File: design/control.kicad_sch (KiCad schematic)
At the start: 22 parts, among them J1 USB_C_Receptacle_USB2.0_14P, J2 SMB, J3 Conn-OScope, J4 Conn-OScope, J5 SMA, U1 CP2102N-Axx-xQFN20, U2 STM32F303RETx

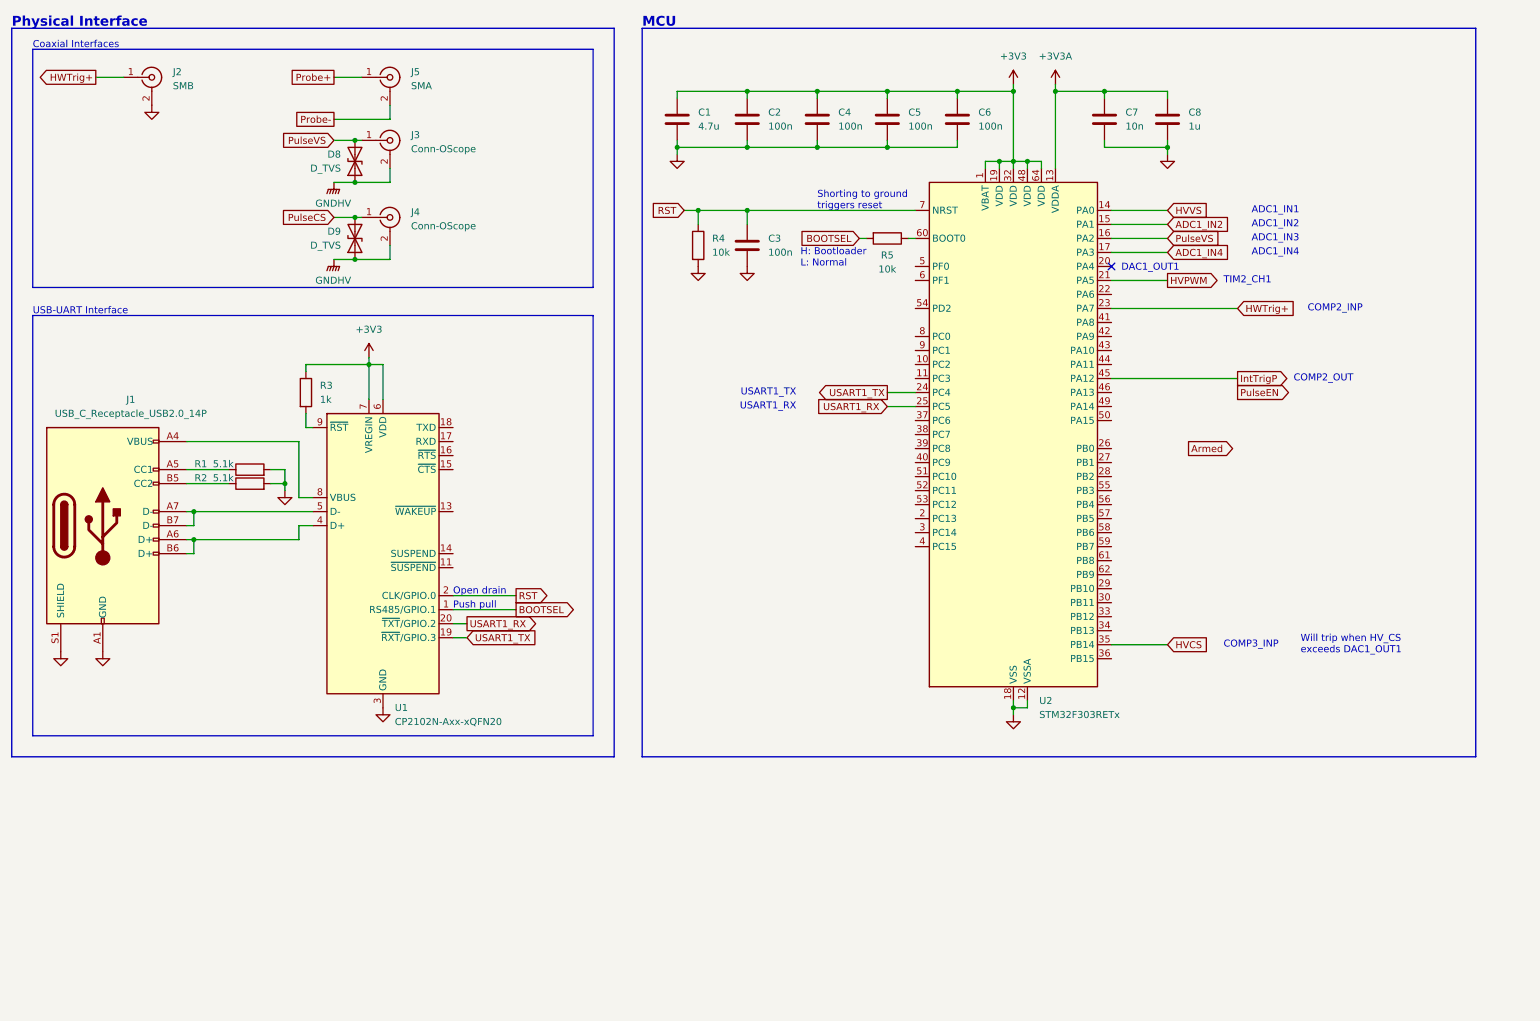
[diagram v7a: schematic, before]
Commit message: Switched to FT230X UART bridge
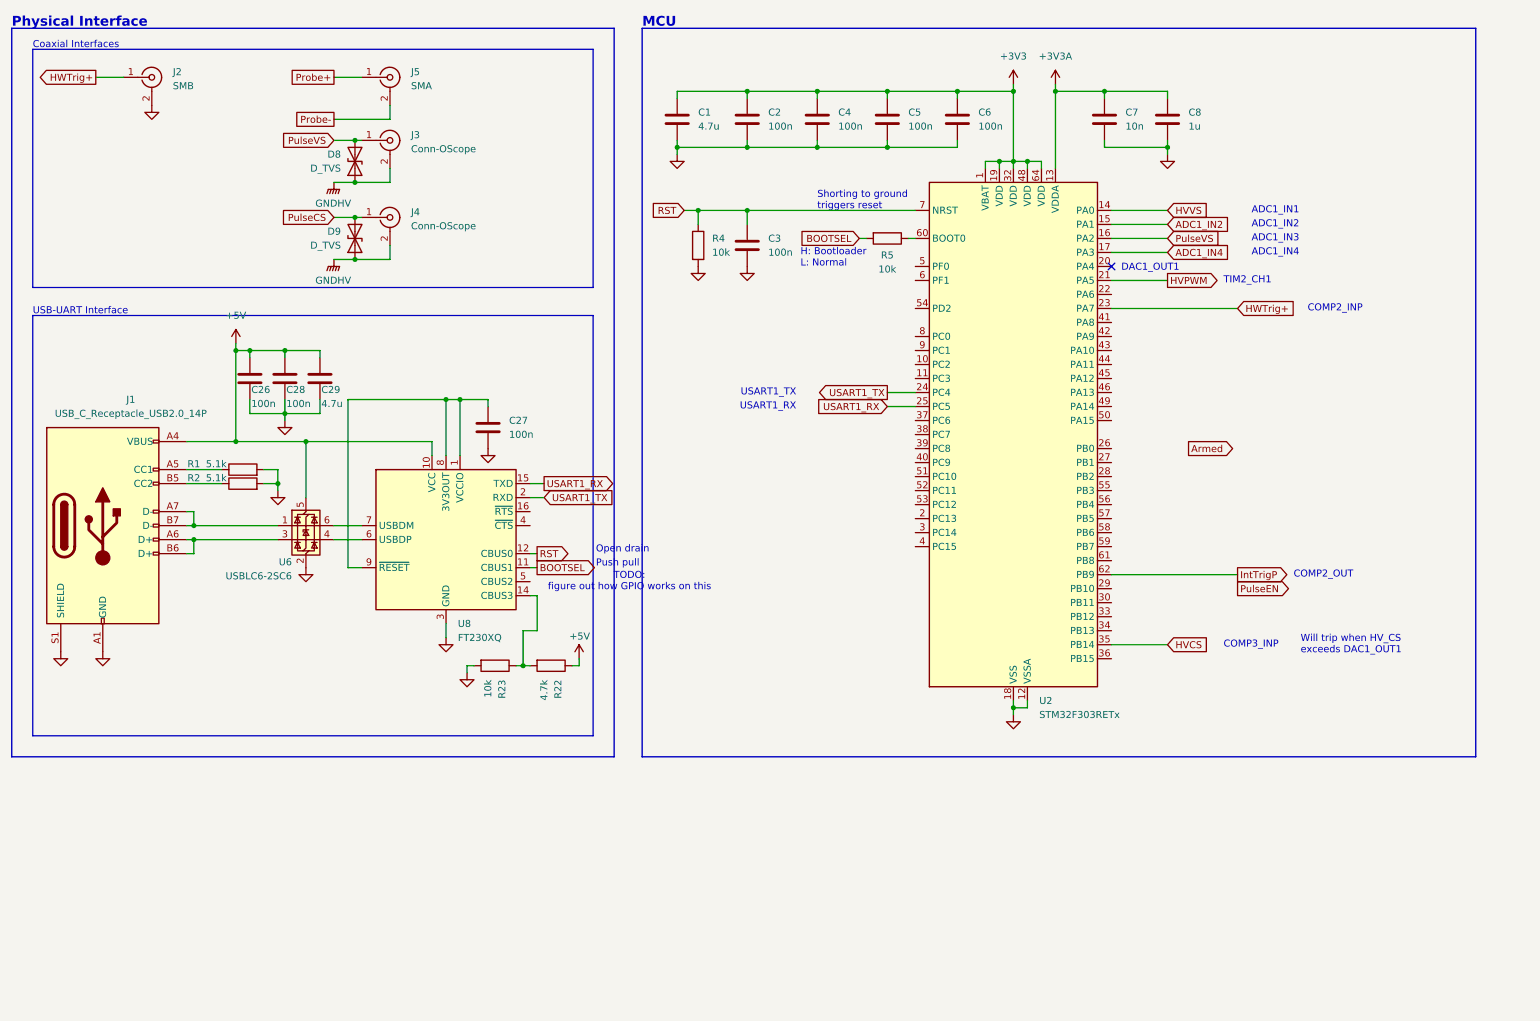
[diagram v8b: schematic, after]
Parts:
- removed R3: 1k, symbol Device:R
- removed U1: CP2102N-Axx-xQFN20, Package_DFN_QFN:SiliconLabs_QFN-20-1EP_3x3mm_P0.5mm, symbol Interface_USB:CP2102N-Axx-xQFN20
- added C26, C27, C28: 100n, symbol Device:C
- added C29: 4.7u, symbol Device:C
- added R22: 4.7k, symbol Device:R
- added R23: 10k, symbol Device:R
- added U6: USBLC6-2SC6, Package_TO_SOT_SMD:SOT-23-6, symbol Power_Protection:USBLC6-2SC6
- added U8: FT230XQ, Package_DFN_QFN:QFN-16-1EP_4x4mm_P0.65mm_EP2.1x2.1mm, symbol Interface_USB:FT230XQ
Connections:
- net BOOTSEL: now also U8.11 (CBUS1)
- net GND: now also C26.2, C27.2, C28.2, C29.2, R23.2, U6.2 (GND), U8.13 (GND), U8.17 (GND), U8.3 (GND)
- net IntTrigP: now also U2.62 (PB9); no longer U2.45 (PA12)
- net RST: now also U8.12 (CBUS0)
- net USART1_RX: now also U8.15 (TXD)
- net USART1_TX: now also U8.2 (RXD)
- net at J1.A6 (D+), J1.B6 (D+): now also U6.3 (I/O2)
- net at J1.A7 (D-), J1.B7 (D-): now also U6.1 (I/O1)
- net +5V: now reaches J1.A4 (VBUS), J1.A9 (VBUS), J1.B4 (VBUS), J1.B9 (VBUS)
- net +5V: now also C26.1, C28.1, C29.1, R22.1, U6.5 (VBUS), U8.10 (VCC)
- new net: C27.1, U8.1 (VCCIO), U8.8 (3V3OUT), U8.9 (~{RESET})
- new net: R22.2, R23.1, U8.14 (CBUS3)
- new net: U6.4 (I/O2), U8.6 (USBDP)
- new net: U6.6 (I/O1), U8.7 (USBDM)
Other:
- note added: "TODO: figure out how GPIO works on this"
- moved on the sheet: R1, R2
